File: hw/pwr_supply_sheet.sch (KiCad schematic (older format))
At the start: 12 parts

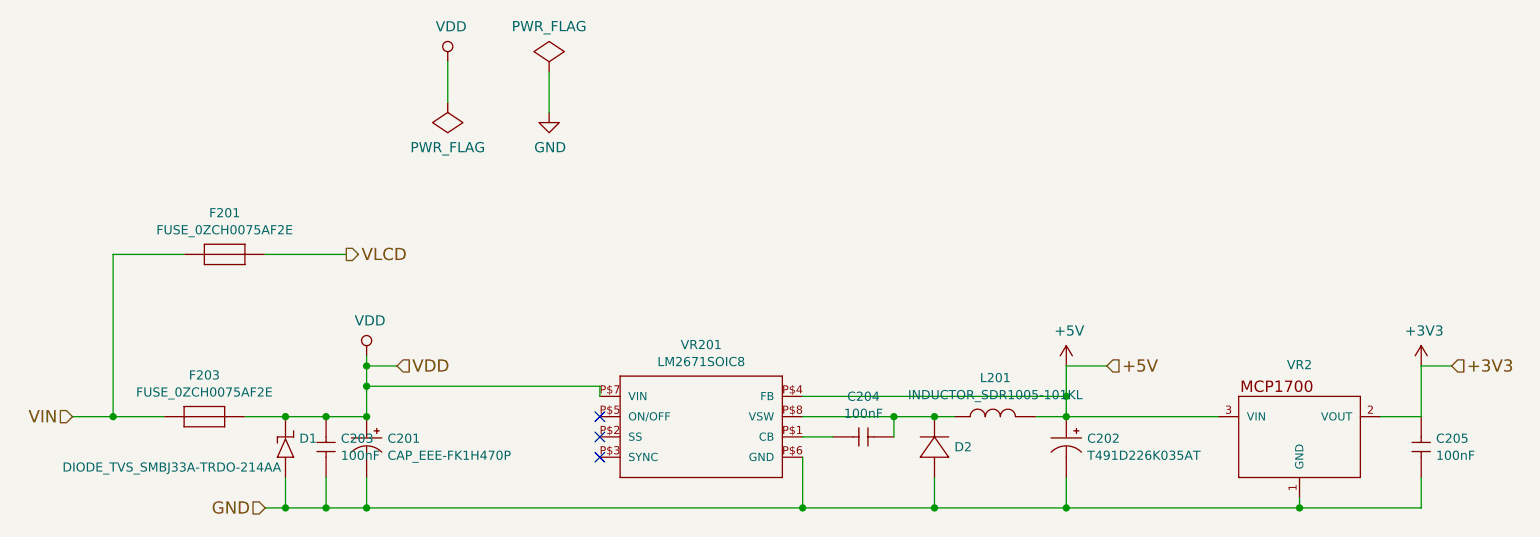
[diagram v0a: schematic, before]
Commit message: displa pcb reverted back to 1.6.0 revision and imporved to 1.7.0
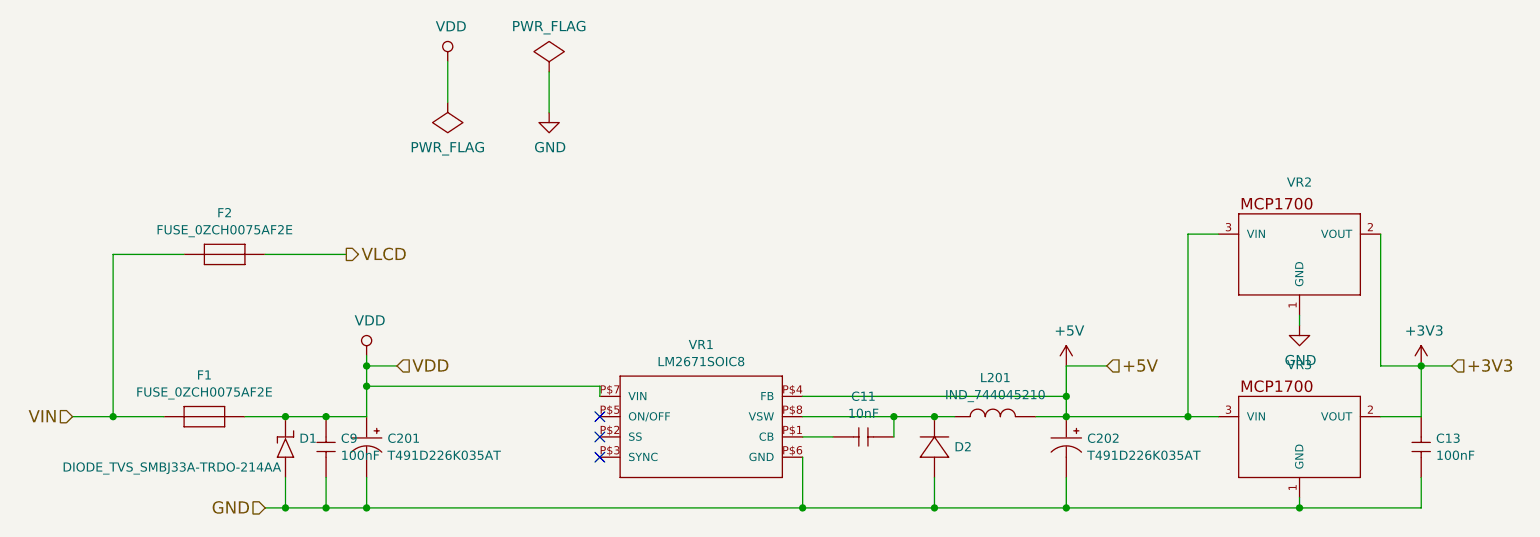
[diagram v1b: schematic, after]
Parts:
- removed C201: CAP_EEE-FK1H470P, usevolt:CAP_EEE-FK1H470P, symbol usevolt:CAP_EEE-FK1H470P
- removed C203, C204, C205: 100nF, kemet:0603, symbol kemet:100nF
- removed F201, F203: FUSE_0ZCH0075AF2E, usevolt:1210, symbol usevolt:FUSE_0ZCH0075AF2E
- removed L201: INDUCTOR_SDR1005-101KL, usevolt:INDUCTOR_BOURNS_10X13X5MM, symbol usevolt:INDUCTOR_SDR1005-101KL
- removed VR201: LM2671SOIC8, usevolt:SOIC8, symbol usevolt:LM2671SOIC8
- added C11: 10nF, kemet:Kemet-CAPC1608X85N, symbol kemet:10nF
- added C13, C9: 100nF, kemet:Kemet-CAPC1608X85N, symbol kemet:100nF
- added C201: T491D226K035AT, kemet:7343, symbol kemet:T491D226K035AT
- added F1, F2: FUSE_0ZCH0075AF2E, usevolt:1210, symbol usevolt:FUSE_0ZCH0075AF2E
- added L201: IND_744045210, usevolt:IND_744045210, symbol usevolt:IND_744045210
- added VR1: LM2671SOIC8, usevolt:SOIC8, symbol display-rescue:LM2671SOIC8
- added VR3: REG_MCP1700, usevolt:SOT-23_3-PIN, symbol usevolt:REG_MCP1700
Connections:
- net +3V3: now also C13.1 (C1), VR3.2 (VOUT)
- net +5V: now also L201.2, VR1.P$4 (FB), VR3.3 (VIN)
- net GND: now also C13.2 (C2), C201.-, C9.2 (C2), VR1.P$6 (GND), VR3.1 (GND)
- net VDD: now also C201.+, C9.1 (C1), F1.2, VR1.P$7 (VIN)
- net VIN: now also F1.1, F2.1
- net VLCD: now also F2.2
- net at D2.P$2 (N): now also C11.2 (C2), L201.1, VR1.P$8 (VSW)
- new net: C11.1 (C1), VR1.P$1 (CB)
